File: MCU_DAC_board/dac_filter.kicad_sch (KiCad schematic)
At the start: 13 parts, among them J1 Conn_02x04_Odd_Even

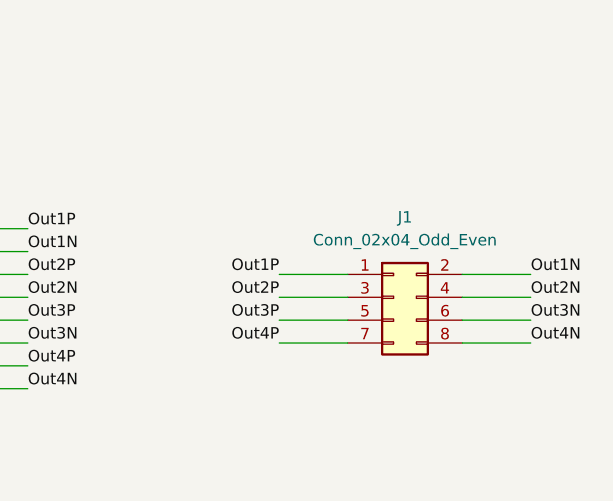
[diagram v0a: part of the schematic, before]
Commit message: Finished layout for DAC board with 1 MCU
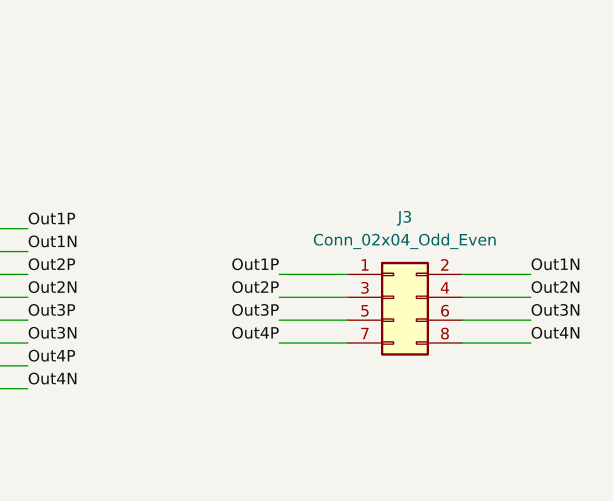
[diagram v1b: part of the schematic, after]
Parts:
- renumbered J1 to J3
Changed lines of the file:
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@@
 		(dnp no)
 		(fields_autoplaced yes)
-		(property "Reference" "J1"
+		(property "Reference" "J3"
 			(at 196.85 83.82 0)
 			(effects

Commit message: Revised DAC board schematic
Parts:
- renumbered C22 to C11, C23 to C12, C24 to C13, C25 to C14, J3 to J1, R18 to R2, R19 to R3, R20 to R4, R21 to R5, R22 to R6, R23 to R7, R24 to R8, R25 to R9
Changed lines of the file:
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@@
 (kicad_sch
-	(version 20231120)
+	(version 20250114)
 	(generator "eeschema")
-	(generator_version "8.0")
+	(generator_version "9.0")
 	(paper "A4")
 	(junction
@@
 	(label "Out2P"
 		(at 154.94 90.17 0)
-		(fields_autoplaced yes)
 		(effects
 			(font
@@
 	(label "Out1N"
 		(at 210.82 90.17 0)
-		(fields_autoplaced yes)
 		(effects
 			(font
@@
 	(label "Out3N"
 		(at 210.82 95.25 0)
-		(fields_autoplaced yes)
 		(effects
 			(font
@@
 	(label "Out4N"
 		(at 154.94 102.87 0)
-		(fields_autoplaced yes)
 		(effects
 			(font
@@
 	(label "Out1P"
 		(at 154.94 85.09 0)
-		(fields_autoplaced yes)
 		(effects
 			(font
@@
 	(label "Out3P"
 		(at 154.94 95.25 0)
-		(fields_autoplaced yes)
 		(effects
 			(font
@@
 	(label "Out2N"
 		(at 154.94 92.71 0)
-		(fields_autoplaced yes)
 		(effects
 			(font
@@
 	(label "Out4P"
 		(at 182.88 97.79 180)
-		(fields_autoplaced yes)
 		(effects
 			(font
@@
 	(label "Out1P"
 		(at 182.88 90.17 180)
-		(fields_autoplaced yes)
 		(effects
 			(font
@@
 	(label "Out1N"
 		(at 154.94 87.63 0)
-		(fields_autoplaced yes)
 		(effects
 			(font
@@
 	(label "Out3N"
 		(at 154.94 97.79 0)
-		(fields_autoplaced yes)
 		(effects
 			(font
@@
 	(label "Out2N"
 		(at 210.82 92.71 0)
-		(fields_autoplaced yes)
 		(effects
 			(font
@@
 	(label "Out4P"
 		(at 154.94 100.33 0)
-		(fields_autoplaced yes)
 		(effects
 			(font
@@
 	(label "Out2P"
 		(at 182.88 92.71 180)
-		(fields_autoplaced yes)
 		(effects
 			(font
@@
 	(label "Out3P"
 		(at 182.88 95.25 180)
-		(fields_autoplaced yes)
 		(effects
 			(font
@@
 	(label "Out4N"
 		(at 210.82 97.79 0)
-		(fields_autoplaced yes)
 		(effects
 			(font
@@
 		(shape input)
 		(at 83.82 82.55 180)
-		(fields_autoplaced yes)
 		(effects
 			(font
@@
 		(shape input)
 		(at 83.82 113.03 180)
-		(fields_autoplaced yes)
 		(effects
 			(font
@@
 		(shape input)
 		(at 83.82 120.65 180)
-		(fields_autoplaced yes)
 		(effects
 			(font
@@
 		(shape input)
 		(at 83.82 67.31 180)
-		(fields_autoplaced yes)
 		(effects
 			(font
@@
 		(shape input)
 		(at 83.82 97.79 180)
-		(fields_autoplaced yes)
 		(effects
 			(font
@@
 		(shape input)
 		(at 83.82 74.93 180)
-		(fields_autoplaced yes)
 		(effects
 			(font
@@
 		(shape input)
 		(at 83.82 90.17 180)
-		(fields_autoplaced yes)
 		(effects
 			(font
@@
 		(shape input)
 		(at 83.82 105.41 180)
-		(fields_autoplaced yes)
 		(effects
 			(font
@@
 		(dnp no)
 		(fields_autoplaced yes)
-		(property "Reference" "C22"
+		(property "Reference" "C11"
 			(at 110.49 69.8562 0)
 			(effects
@@
 		(on_board yes)
 		(dnp no)
-		(property "Reference" "R25"
+		(property "Reference" "R9"
 			(at 99.06 116.84 90)
 			(effects
@@
 		(dnp no)
 		(fields_autoplaced yes)
-		(property "Reference" "C25"
+		(property "Reference" "C14"
 			(at 110.49 115.5762 0)
 			(effects
@@
 		(on_board yes)
 		(dnp no)
-		(property "Reference" "R21"
+		(property "Reference" "R5"
 			(at 99.06 86.36 90)
 			(effects
@@
 		(on_board yes)
 		(dnp no)
-		(property "Reference" "R18"
+		(property "Reference" "R2"
 			(at 99.06 62.992 90)
 			(effects
@@
 		(dnp no)
 		(fields_autoplaced yes)
-		(property "Reference" "J3"
+		(property "Reference" "J1"
 			(at 196.85 83.82 0)
 			(effects
@@
 		(on_board yes)
 		(dnp no)
-		(property "Reference" "R22"
+		(property "Reference" "R6"
 			(at 99.06 93.472 90)
 			(effects
@@
 		(on_board yes)
 		(dnp no)
-		(property "Reference" "R24"
+		(property "Reference" "R8"
 			(at 99.06 108.712 90)
 			(effects
@@
 		(dnp no)
 		(fields_autoplaced yes)
-		(property "Reference" "C24"
+		(property "Reference" "C13"
 			(at 110.49 100.3362 0)
 			(effects
@@
 		(on_board yes)
 		(dnp no)
-		(property "Reference" "R23"
+		(property "Reference" "R7"
 			(at 99.06 101.6 90)
 			(effects
@@
 		(dnp no)
 		(fields_autoplaced yes)
-		(property "Reference" "C23"
+		(property "Reference" "C12"
 			(at 110.49 85.0962 0)
 			(effects
@@
 		(on_board yes)
 		(dnp no)
-		(property "Reference" "R19"
+		(property "Reference" "R3"
 			(at 99.06 71.12 90)
 			(effects
@@
 		(on_board yes)
 		(dnp no)
-		(property "Reference" "R20"
+		(property "Reference" "R4"
 			(at 99.06 78.232 90)
 			(effects
